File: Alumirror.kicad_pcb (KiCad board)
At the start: 2 copper layers, 139.7 x 88.9 mm, 96 parts, among them J1 USB_C_Receptacle_USB2.0_16P_2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, J2 USB_C_Receptacle_USB2.0_16P_2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, J3 USB_C_Receptacle_USB2.0_16P_2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, J4 USB_C_Receptacle_USB2.0_16P_2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, K11 PG1350, K12 PG1350, K13 PG1350, K14 PG1350, K15 PG1350, K16 PG1350, K21 PG1350, K22 PG1350, K23 PG1350, K24 PG1350, K25 PG1350, K26 PG1350, K31 PG1350, K32 PG1350, K33 PG1350, K34 PG1350, K35 PG1350, K36 PG1350_1½U, K41 PG1350_1½U, K42 PG1350/SKQUCAA010, SW10 BOOT, U1 CH552T, U2 CH552T, U3 USBLC6-2P6, U4 USBLC6-2P6, U5 USBLC6-2P6, U6 USBLC6-2P6

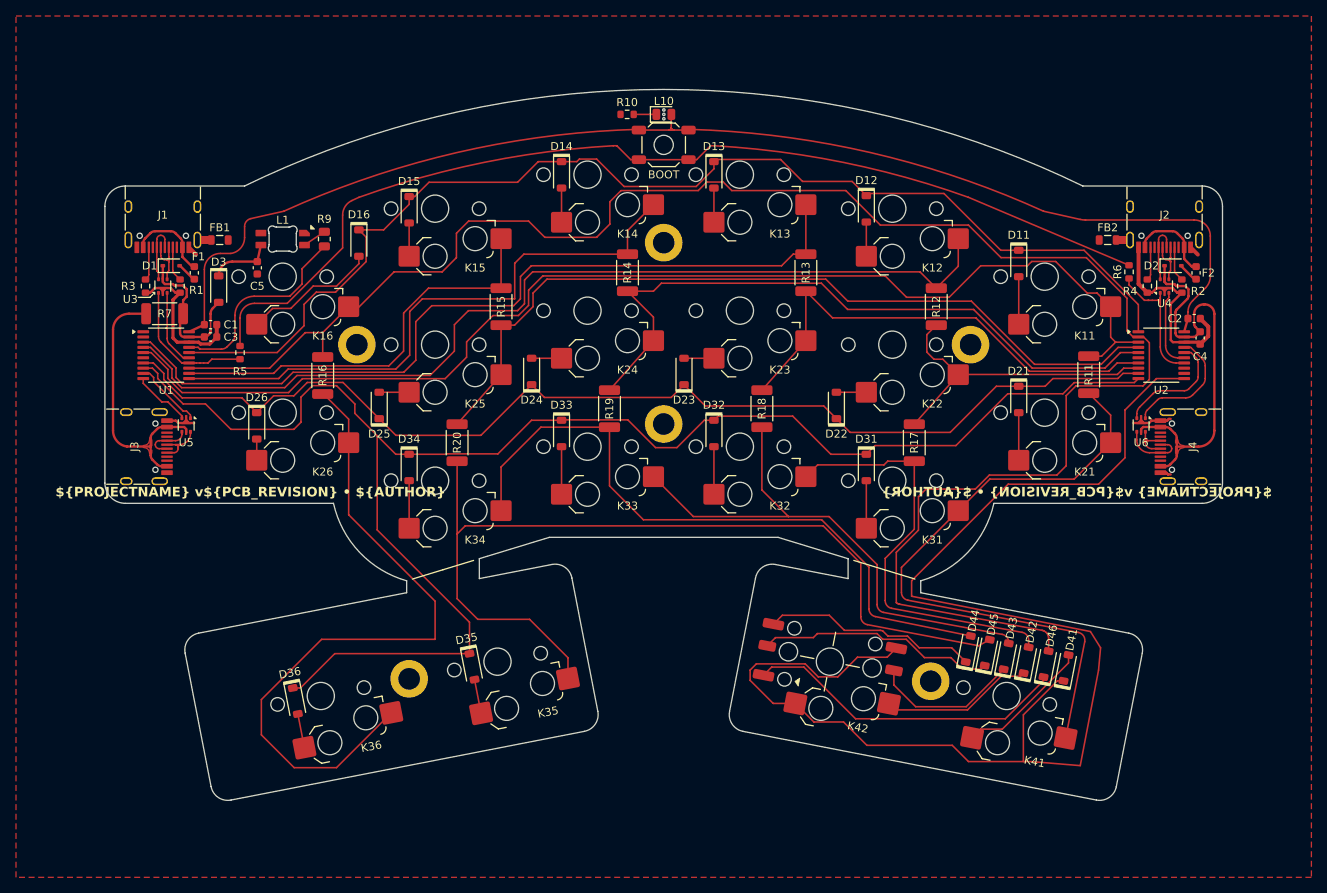
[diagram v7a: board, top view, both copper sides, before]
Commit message: Clean up cross-board column routing
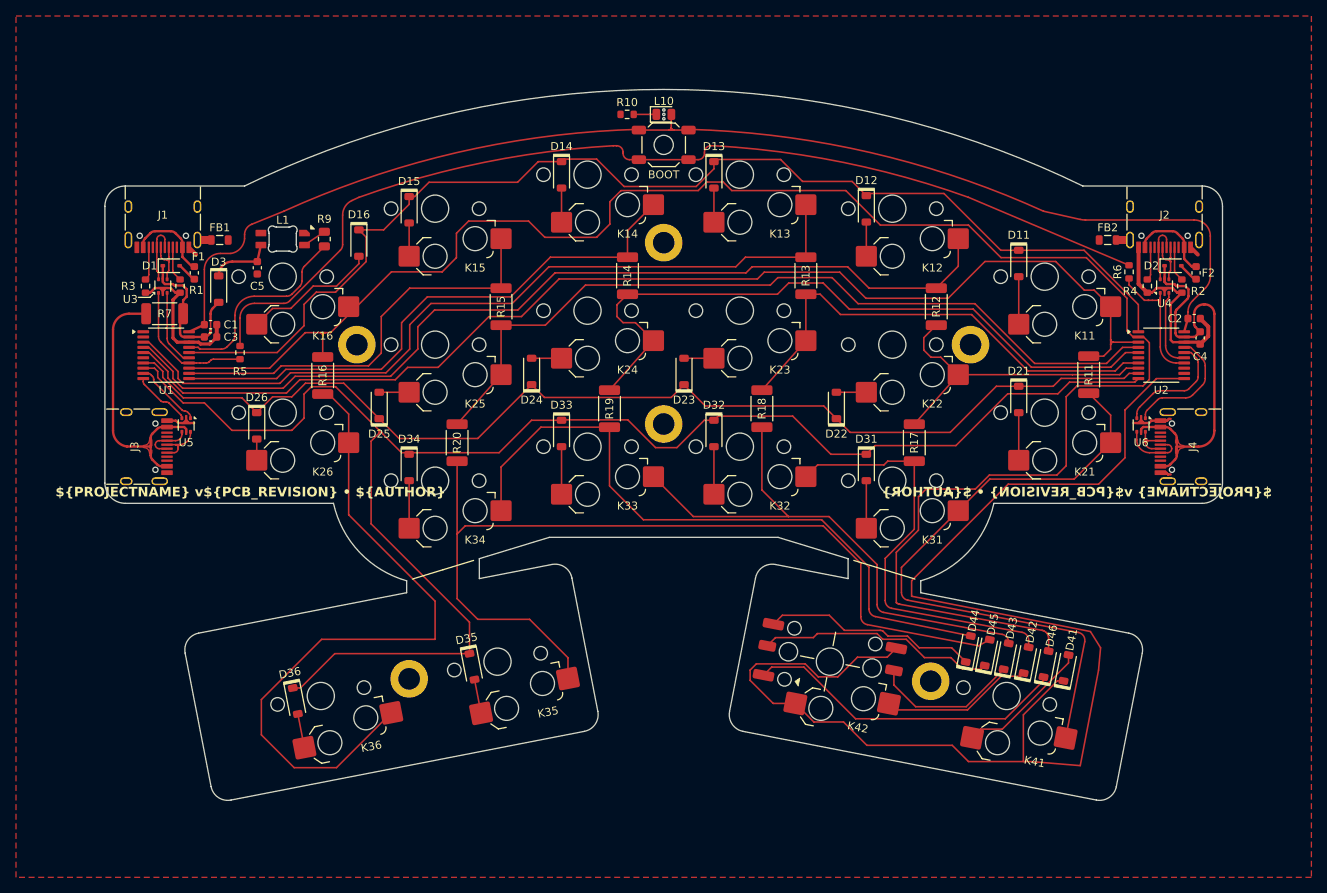
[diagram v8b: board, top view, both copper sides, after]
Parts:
- moved R13 0.38 mm to (170.2, 52.3)
- moved R14 0.38 mm to (147.9, 52.3)
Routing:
- net Col4L: track 74.6 -> 70.9 mm
- net Col3L: track 103.0 -> 100.4 mm
- net Col1: track 148.9 -> 146.3 mm
- net Col4R: track 85.3 -> 87.0 mm
- net Col2L: track 119.7 -> 118.1 mm
- net Col5R: track 102.8 -> 101.9 mm
- net Col6: track 229.2 -> 228.2 mm
- net TX_L: track 8.75 -> 8.03 mm
- net +3V3: track 65.5 -> 64.9 mm
- net Col3R: track 60.6 -> 60.0 mm
